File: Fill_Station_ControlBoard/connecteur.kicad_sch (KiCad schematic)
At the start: 1 part, among them J2 Conn_02x05_Counter_Clockwise

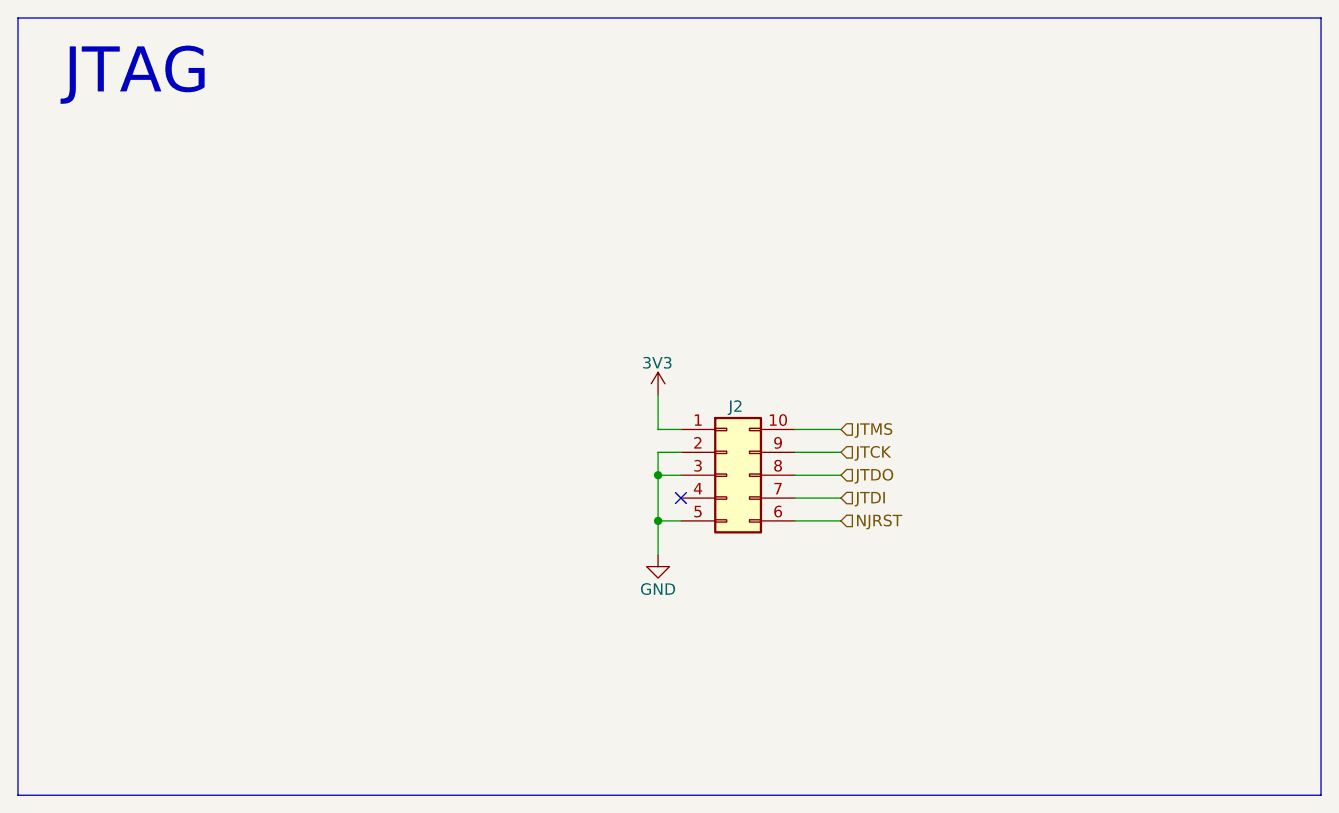
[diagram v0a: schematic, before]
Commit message: Changement de CAN et quelques trucs
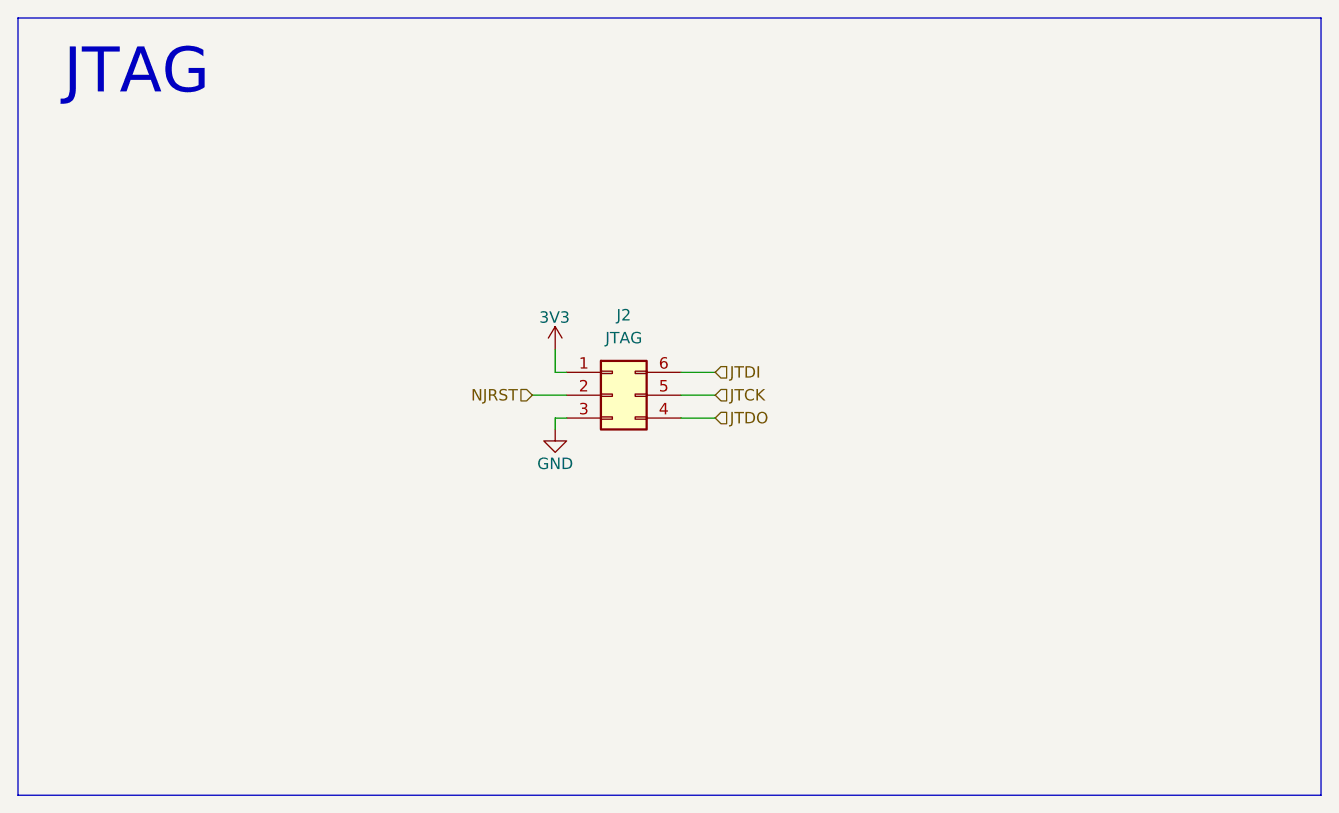
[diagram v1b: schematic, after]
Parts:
- removed J2: Conn_02x05_Counter_Clockwise, symbol Connector_Generic:Conn_02x05_Counter_Clockwise
- added J2: JTAG, UserFootprints:490107670612, symbol Connector_Generic:Conn_02x03_Counter_Clockwise
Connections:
- net 3V3: now also J2.1 (Pin_1)
- net GND: now also J2.3 (Pin_3)
- net JTCK: now also J2.5 (Pin_5)
- net JTDI: now also J2.6 (Pin_6)
- net JTDO: now also J2.4 (Pin_4)
- net NJRST: now also J2.2 (Pin_2)
- no-connect marks 1 -> 0

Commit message: Vince
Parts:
- removed J2: JTAG, UserFootprints:490107670612, symbol Connector_Generic:Conn_02x03_Counter_Clockwise
- added J4: Conn_02x05_Counter_Clockwise, symbol Connector_Generic:Conn_02x05_Counter_Clockwise
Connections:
- net 3V3: now also J4.1 (Pin_1)
- net GND: now also J4.2 (Pin_2), J4.3 (Pin_3), J4.5 (Pin_5)
- net JTCK: now also J4.9 (Pin_9)
- net JTDI: now also J4.7 (Pin_7)
- net JTDO: now also J4.8 (Pin_8)
- net NJRST: now also J4.6 (Pin_6)
- new net JTMS: J4.10 (Pin_10)
- no-connect marks 0 -> 1
